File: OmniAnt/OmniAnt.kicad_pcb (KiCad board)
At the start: 4 copper layers, 115 parts, among them J1 Connector, USB-TYPE-C-16P, J10 Conn_01x01, J11 Conn_01x01, J12 Conn_01x01, J13 Conn_01x01, J14 Conn_01x01, J15 Conn_01x01, J16 Conn_01x01, J17 Conn_01x01, J18 Conn_01x01, J19 Conn_01x01, J2 Conn_01x02_Pin, J20 Conn_01x01, J21 Conn_01x01, J22 Conn_01x01, J23 Conn_01x01, J24 Conn_01x01, J25 Conn_01x01, J26 Conn_01x01, J27 Conn_01x01, J28 Conn_01x01, J29 Conn_01x01, J3 Conn_01x04_Pin, J30 Conn_01x01, J31 Conn_01x01, J32 Conn_01x01, J33 Conn_01x01, J34 Conn_01x01, J35 Conn_01x01, J36 Conn_01x01, J37 Conn_01x01, J38 Conn_01x01, J39 Conn_01x01, J4 XT30PW-M, J5 XT30PW-M, J6 XT30PW-M, J7 XT30PW-M, J8 Conn_01x01, J9 Conn_01x01, Q1 NTMFS4C324NT1G, Q10 NTMFS4C324NT1G, Q11 NTMFS4C324NT1G, Q12 NTMFS4C324NT1G, Q2 NTMFS4C324NT1G, Q3 NTMFS4C324NT1G, Q4 NTMFS4C324NT1G, Q5 NTMFS4C324NT1G, Q6 NTMFS4C324NT1G, Q7 NTMFS4C324NT1G, Q8 NTMFS4C324NT1G, Q9 NTMFS4C324NT1G, U1 USBLC6-2P6, U2 TPSM53603RDA, U3 ESP32-S3-WROOM-1, U4 MCF8329A1IREER, U5 MCF8329A1IREER

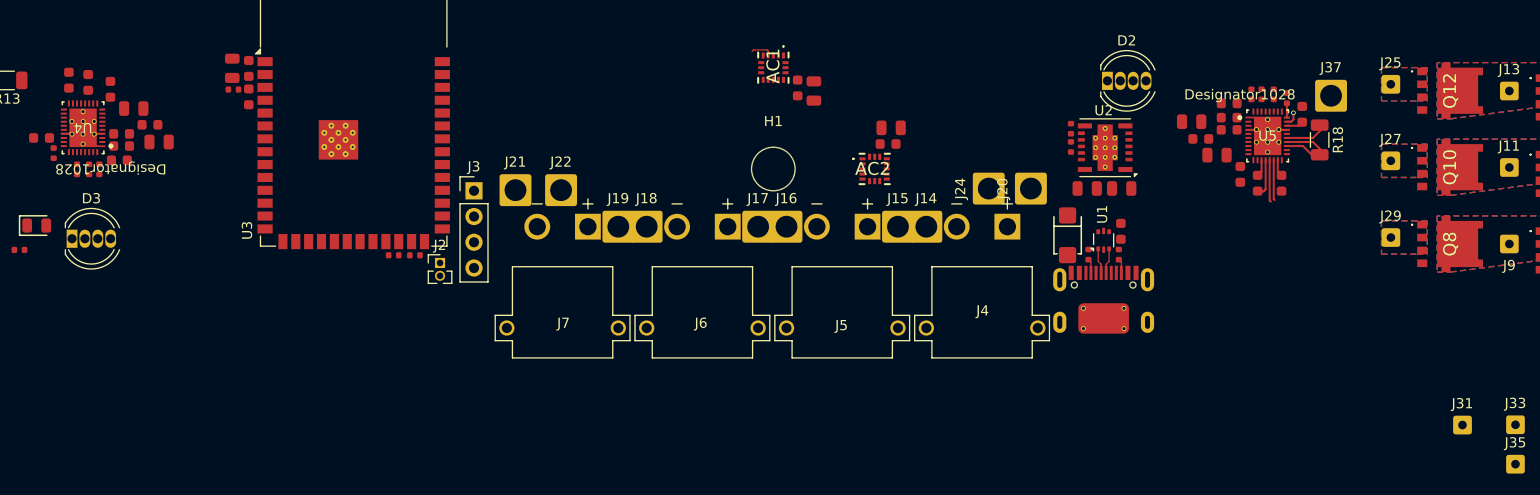
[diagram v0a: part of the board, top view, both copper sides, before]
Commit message: I made more progress on the layout. I'm working on adding the extra protection components to the driver circuit.
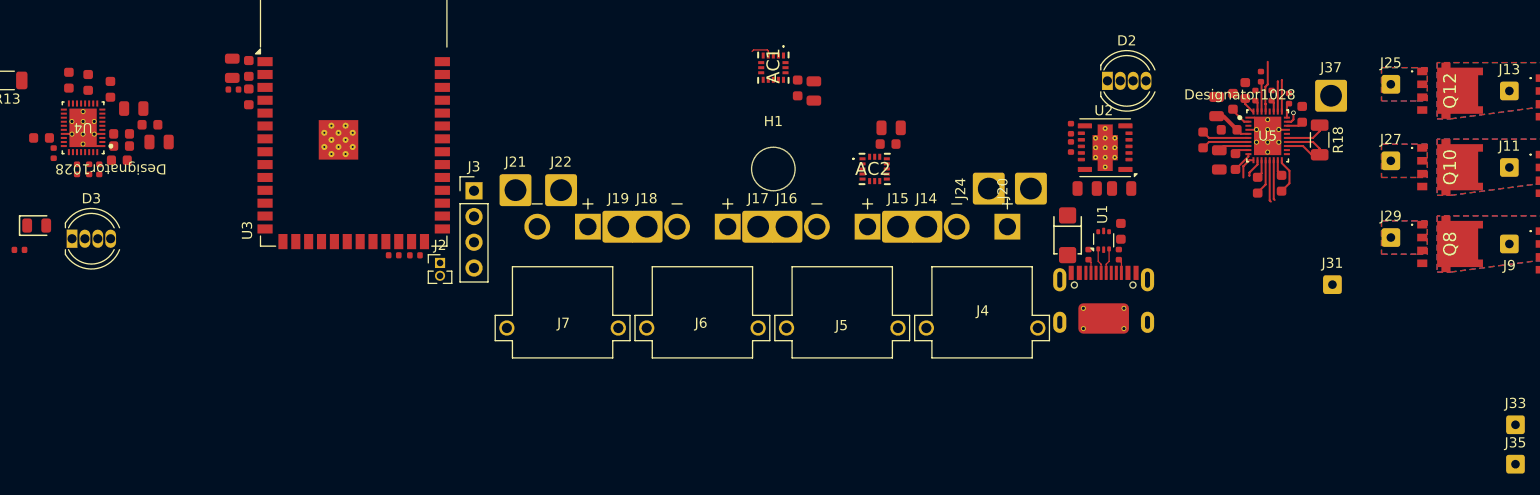
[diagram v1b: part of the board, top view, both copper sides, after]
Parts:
- moved J31 18.9 mm to (257.3, 35.2)
- moved C20 2.88 mm to (245.8, 17.6), turned to 90 degrees
- moved C18 2.03 mm to (248.7, 16.0), turned to 90 degrees
- moved R14 1.75 mm to (250.2, 14.7)
- moved C22 1.66 mm to (247.5, 17.1), turned to 90 degrees
- moved C24 1.36 mm to (247.7, 23.0)
- moved C19 0.52 mm to (246.1, 22.9), turned to -90 degrees
- moved R16 0.41 mm to (249.7, 16.5)
- moved C23 0.25 mm to (244.5, 20.9), turned to 90 degrees
- moved R15 0.24 mm to (251.3, 16.5)
- moved R17 0.21 mm to (253.0, 16.8)
- moved C26 0.19 mm to (249.9, 25.4)
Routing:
- net /Motor2_DAC: track 0.00 -> 5.02 mm
- net Net-(U5-CPL): track 0.00 -> 4.71 mm
- net Net-(U5-CPH): track 0.00 -> 4.71 mm
- net /Batt: track 0.00 -> 3.86 mm
- net /Motor2/PhaseC: track 0.00 -> 3.68 mm
- net /I2C_SDA: track 0.00 -> 3.10 mm
- net Net-(U5-GVDD): track 0.00 -> 3.04 mm
- net /I2C_SCL: track 0.00 -> 2.98 mm
- net Net-(U5-BRAKE): track 0.00 -> 2.97 mm
- net Net-(Q7-G): track 0.00 -> 2.36 mm
- net +3.3V: track 0.00 -> 2.11 mm
- net /Motor2/PhaseA: track 0.00 -> 2.04 mm
- net Net-(Q8-G): track 0.00 -> 1.86 mm
- net Net-(U5-DVDD): track 0.00 -> 1.68 mm
- net Net-(U5-BSTA): track 0.00 -> 1.42 mm
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
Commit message: Ok I did a lot of reading today. I'm going to split each FET into a sheet, so I can add the external circuitry more easily.
I may need to source a different FET. The one I selected has a good EAS, but the rating is only for 11A. and Ideally I would be able to do 19 or 20A. I'm sure I will never do that much current , but relying on the mosfet to handle things seems better than adding an additional tvs diode. Snubber is the way to go for sure to keep things cool.
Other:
- board text added: "TODO: Add mounting / locating holes for the motor. Make the gate traces 0.5mm"
- board text removed: "TODO: Add solder wire connections for the busbar wires. Add mounting / locating holes for the motor. Add boxes to represent the batteries."
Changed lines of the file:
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@@
 		(layer "User.1")
 	)
-	(gr_text "TODO: \nAdd solder wire connections for the busbar wires. \nAdd mounting / locating holes for the motor. \nAdd boxes to represent the batteries. \n"
+	(gr_text "TODO: \nAdd mounting / locating holes for the motor. \nMake the gate traces 0.5mm\n"
 		(at 179.3 173.5 0)
 		(layer "Cmts.User")
@@
 			(font
 				(size 1 1)
-				(thickness 0.15)
+				(thickness 0.125)
 			)
 			(justify left bottom)

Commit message: Well shit making the FETs into libraries totally screwed up the annotation :( I decided to just redo the layout for the FETs anyhow.
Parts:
- removed Q1, Q10, Q11, Q12, Q2, Q3, Q4, Q5, Q6, Q7, Q8, Q9: NTMFS4C324NT1G, Footprints:NVMFS5C442NLWFAFT1G
- added C1001: 470pF, PCM_JLCPCB:C_0603, F.Cu at (9.08, -38.9)
- added C1101: 470pF, PCM_JLCPCB:C_0603, F.Cu at (85.4, 124.3)
- added C1201: 470pF, PCM_JLCPCB:C_0603, F.Cu at (66.6, 161.3)
- added C1301: 470pF, PCM_JLCPCB:C_0603, F.Cu at (-9.68, -20.4)
- added C1401: 470pF, PCM_JLCPCB:C_0603, F.Cu at (-9.68, -38.9)
- added C1501: 470pF, PCM_JLCPCB:C_0603, F.Cu at (66.6, 142.8)
- added C1601: 470pF, PCM_JLCPCB:C_0603, F.Cu at (104.2, 124.3)
- added C1701: 470pF, PCM_JLCPCB:C_0603, F.Cu at (66.6, 179.8)
- added C211: 100nF, PCM_JLCPCB:C_0603, F.Cu at (50.6, -40.8)
- added C212: 100nF, PCM_JLCPCB:C_0603, F.Cu at (50.6, -38.5)
- added C213: 100nF, PCM_JLCPCB:C_0603, F.Cu at (50.6, -36.3)
- added C214: C_US, Capacitor_THT:CP_Radial_D6.3mm_P2.50mm, F.Cu at (43.5, -38.0)
- added C215: C_US, Capacitor_THT:CP_Radial_D6.3mm_P2.50mm, F.Cu at (43.5, -30.1)
- added C216: C_US, Capacitor_THT:CP_Radial_D6.3mm_P2.50mm, F.Cu at (43.5, -22.3)
- added C311: 100nF, PCM_JLCPCB:C_0603, F.Cu at (49.3, 112.3)
- added C312: 100nF, PCM_JLCPCB:C_0603, F.Cu at (49.3, 114.5)
- added C313: 100nF, PCM_JLCPCB:C_0603, F.Cu at (49.3, 116.8)
- added C314: C_US, Capacitor_THT:CP_Radial_D6.3mm_P2.50mm, F.Cu at (42.2, 115.1)
- added C315: C_US, Capacitor_THT:CP_Radial_D6.3mm_P2.50mm, F.Cu at (42.2, 122.9)
- added C316: C_US, Capacitor_THT:CP_Radial_D6.3mm_P2.50mm, F.Cu at (42.2, 130.8)
- added C601: 470pF, PCM_JLCPCB:C_0603, F.Cu at (9.08, -20.4)
- added C701: 470pF, PCM_JLCPCB:C_0603, F.Cu at (-9.68, -57.4)
- added C801: 470pF, PCM_JLCPCB:C_0603, F.Cu at (66.6, 124.3)
- added C901: 470pF, PCM_JLCPCB:C_0603, F.Cu at (9.08, -57.4)
- added D1001: 1N5819WS, PCM_JLCPCB:D_SOD-323, F.Cu at (9.34, -41.5)
- added D1002: SMAJ13A, PCM_JLCPCB:D_SMA, F.Cu at (8.39, -49.8)
- added D1003: SMAJ18CA, PCM_JLCPCB:D_SMA, F.Cu at (8.39, -45.3)
- added D1101: 1N5819WS, PCM_JLCPCB:D_SOD-323, F.Cu at (85.7, 121.7)
- added D1102: SMAJ13A, PCM_JLCPCB:D_SMA, F.Cu at (84.7, 118.0)
- added D1103: SMAJ18CA, PCM_JLCPCB:D_SMA, F.Cu at (84.7, 113.4)
- added D1201: 1N5819WS, PCM_JLCPCB:D_SOD-323, F.Cu at (66.9, 158.7)
- added D1202: SMAJ13A, PCM_JLCPCB:D_SMA, F.Cu at (65.9, 155.0)
- added D1203: SMAJ18CA, PCM_JLCPCB:D_SMA, F.Cu at (65.9, 150.4)
- added D1301: 1N5819WS, PCM_JLCPCB:D_SOD-323, F.Cu at (-9.42, -23.0)
- added D1302: SMAJ13A, PCM_JLCPCB:D_SMA, F.Cu at (-10.4, -31.3)
- added D1303: SMAJ18CA, PCM_JLCPCB:D_SMA, F.Cu at (-10.4, -26.8)
- added D1401: 1N5819WS, PCM_JLCPCB:D_SOD-323, F.Cu at (-9.42, -41.5)
- added D1402: SMAJ13A, PCM_JLCPCB:D_SMA, F.Cu at (-10.4, -45.3)
- added D1403: SMAJ18CA, PCM_JLCPCB:D_SMA, F.Cu at (-10.4, -49.8)
- added D1501: 1N5819WS, PCM_JLCPCB:D_SOD-323, F.Cu at (66.9, 140.2)
- added D1502: SMAJ13A, PCM_JLCPCB:D_SMA, F.Cu at (65.9, 136.5)
- added D1503: SMAJ18CA, PCM_JLCPCB:D_SMA, F.Cu at (65.9, 131.9)
- added D1601: 1N5819WS, PCM_JLCPCB:D_SOD-323, F.Cu at (104.4, 121.7)
- added D1602: SMAJ13A, PCM_JLCPCB:D_SMA, F.Cu at (103.5, 118.0)
- added D1603: SMAJ18CA, PCM_JLCPCB:D_SMA, F.Cu at (103.5, 113.4)
- added D1701: 1N5819WS, PCM_JLCPCB:D_SOD-323, F.Cu at (66.9, 177.2)
- added D1702: SMAJ13A, PCM_JLCPCB:D_SMA, F.Cu at (65.9, 173.5)
- added D1703: SMAJ18CA, PCM_JLCPCB:D_SMA, F.Cu at (65.9, 168.9)
- added D601: 1N5819WS, PCM_JLCPCB:D_SOD-323, F.Cu at (9.34, -23.0)
- added D602: SMAJ13A, PCM_JLCPCB:D_SMA, F.Cu at (8.39, -26.8)
- added D603: SMAJ18CA, PCM_JLCPCB:D_SMA, F.Cu at (8.39, -31.3)
- added D701: 1N5819WS, PCM_JLCPCB:D_SOD-323, F.Cu at (-9.42, -60.0)
- added D702: SMAJ13A, PCM_JLCPCB:D_SMA, F.Cu at (-10.4, -68.3)
- added D703: SMAJ18CA, PCM_JLCPCB:D_SMA, F.Cu at (-10.4, -63.8)
- added D801: 1N5819WS, PCM_JLCPCB:D_SOD-323, F.Cu at (66.9, 121.7)
- added D802: SMAJ13A, PCM_JLCPCB:D_SMA, F.Cu at (65.9, 118.0)
- added D803: SMAJ18CA, PCM_JLCPCB:D_SMA, F.Cu at (65.9, 113.4)
- added D901: 1N5819WS, PCM_JLCPCB:D_SOD-323, F.Cu at (9.34, -60.0)
- added D902: SMAJ13A, PCM_JLCPCB:D_SMA, F.Cu at (8.39, -68.3)
- added D903: SMAJ18CA, PCM_JLCPCB:D_SMA, F.Cu at (8.39, -63.8)
- added QHA701: NTMFS4C324NT1G, Footprints:NVMFS5C442NLWFAFT1G, F.Cu at (-18.8, -65.8)
- added QHA801: NTMFS4C324NT1G, Footprints:NVMFS5C442NLWFAFT1G, F.Cu at (57.5, 116.0)
- added QHB1001: NTMFS4C324NT1G, Footprints:NVMFS5C442NLWFAFT1G, F.Cu at (-0.02, -47.3)
- added QHB1201: NTMFS4C324NT1G, Footprints:NVMFS5C442NLWFAFT1G, F.Cu at (57.5, 153.0)
- added QHC1401: NTMFS4C324NT1G, Footprints:NVMFS5C442NLWFAFT1G, F.Cu at (-18.8, -47.3)
- added QHC1601: NTMFS4C324NT1G, Footprints:NVMFS5C442NLWFAFT1G, F.Cu at (95.1, 116.0)
- added QLA1701: NTMFS4C324NT1G, Footprints:NVMFS5C442NLWFAFT1G, F.Cu at (57.5, 171.5)
- added QLA601: NTMFS4C324NT1G, Footprints:NVMFS5C442NLWFAFT1G, F.Cu at (-0.02, -28.8)
- added QLB1101: NTMFS4C324NT1G, Footprints:NVMFS5C442NLWFAFT1G, F.Cu at (76.3, 116.0)
- added QLB901: NTMFS4C324NT1G, Footprints:NVMFS5C442NLWFAFT1G, F.Cu at (-0.02, -65.8)
- added QLC1301: NTMFS4C324NT1G, Footprints:NVMFS5C442NLWFAFT1G, F.Cu at (-18.8, -28.8)
- added QLC1501: NTMFS4C324NT1G, Footprints:NVMFS5C442NLWFAFT1G, F.Cu at (57.5, 134.5)
- added R1001: 22Ω, PCM_JLCPCB:R_0402, F.Cu at (5.73, -42.1)
- added R1002: 100kΩ, PCM_JLCPCB:R_0402, F.Cu at (5.73, -40.2)
- added R1003: 0Ω, PCM_JLCPCB:R_0402, F.Cu at (5.73, -38.4)
- added R1101: 22Ω, PCM_JLCPCB:R_0402, F.Cu at (82.0, 121.2)
- added R1102: 22Ω, PCM_JLCPCB:R_0402, F.Cu at (82.0, 123.0)
- added R1103: 100kΩ, PCM_JLCPCB:R_0402, F.Cu at (82.0, 124.9)
- added R1104: 0Ω, PCM_JLCPCB:R_0402, F.Cu at (82.0, 126.7)
- added R1201: 22Ω, PCM_JLCPCB:R_0402, F.Cu at (63.3, 158.2)
- added R1202: 22Ω, PCM_JLCPCB:R_0402, F.Cu at (63.3, 160.0)
- added R1203: 100kΩ, PCM_JLCPCB:R_0402, F.Cu at (63.3, 161.9)
- added R1204: 0Ω, PCM_JLCPCB:R_0402, F.Cu at (63.3, 163.7)
- added R1301: 22Ω, PCM_JLCPCB:R_0402, F.Cu at (-13.0, -23.6)
- added R1302: 22Ω, PCM_JLCPCB:R_0402, F.Cu at (-13.0, -21.7)
- added R1303: 100kΩ, PCM_JLCPCB:R_0402, F.Cu at (-13.0, -19.9)
- added R1304: 0Ω, PCM_JLCPCB:R_0402, F.Cu at (-13.0, -18.0)
- added R1401: 22Ω, PCM_JLCPCB:R_0402, F.Cu at (-13.0, -42.1)
- added R1402: 22Ω, PCM_JLCPCB:R_0402, F.Cu at (-13.0, -40.2)
- added R1403: 100kΩ, PCM_JLCPCB:R_0402, F.Cu at (-13.0, -38.4)
- added R1404: 0Ω, PCM_JLCPCB:R_0402, F.Cu at (-13.0, -36.5)
- added R1501: 22Ω, PCM_JLCPCB:R_0402, F.Cu at (63.3, 139.7)
- added R1502: 22Ω, PCM_JLCPCB:R_0402, F.Cu at (63.3, 141.5)
- added R1503: 100kΩ, PCM_JLCPCB:R_0402, F.Cu at (63.3, 143.4)
- added R1504: 0Ω, PCM_JLCPCB:R_0402, F.Cu at (63.3, 145.2)
- added R1601: 22Ω, PCM_JLCPCB:R_0402, F.Cu at (100.8, 121.2)
- added R1602: 22Ω, PCM_JLCPCB:R_0402, F.Cu at (100.8, 123.0)
- added R1603: 100kΩ, PCM_JLCPCB:R_0402, F.Cu at (100.8, 124.9)
- added R1604: 0Ω, PCM_JLCPCB:R_0402, F.Cu at (100.8, 126.7)
- added R1701: 22Ω, PCM_JLCPCB:R_0402, F.Cu at (63.3, 176.7)
- added R1702: 22Ω, PCM_JLCPCB:R_0402, F.Cu at (63.3, 178.5)
- added R1703: 100kΩ, PCM_JLCPCB:R_0402, F.Cu at (63.3, 180.4)
- added R1704: 0Ω, PCM_JLCPCB:R_0402, F.Cu at (63.3, 182.2)
- added R601: 22Ω, PCM_JLCPCB:R_0402, F.Cu at (5.73, -23.6)
- added R602: 22Ω, PCM_JLCPCB:R_0402, F.Cu at (5.73, -21.7)
- added R603: 100kΩ, PCM_JLCPCB:R_0402, F.Cu at (5.73, -19.9)
- added R604: 0Ω, PCM_JLCPCB:R_0402, F.Cu at (5.73, -18.0)
- added R701: 22Ω, PCM_JLCPCB:R_0402, F.Cu at (-13.0, -60.6)
- added R702: 22Ω, PCM_JLCPCB:R_0402, F.Cu at (-13.0, -58.7)
- added R703: 100kΩ, PCM_JLCPCB:R_0402, F.Cu at (-13.0, -56.9)
- added R704: 0Ω, PCM_JLCPCB:R_0402, F.Cu at (-13.0, -55.0)
- added R801: 22Ω, PCM_JLCPCB:R_0402, F.Cu at (63.3, 121.2)
- added R802: 22Ω, PCM_JLCPCB:R_0402, F.Cu at (63.3, 123.0)
- added R803: 100kΩ, PCM_JLCPCB:R_0402, F.Cu at (63.3, 124.9)
- added R804: 0Ω, PCM_JLCPCB:R_0402, F.Cu at (63.3, 126.7)
- added R901: 22Ω, PCM_JLCPCB:R_0402, F.Cu at (5.73, -60.6)
- added R902: 22Ω, PCM_JLCPCB:R_0402, F.Cu at (5.73, -58.7)
- added R903: 100kΩ, PCM_JLCPCB:R_0402, F.Cu at (5.73, -56.9)
- added R904: 0Ω, PCM_JLCPCB:R_0402, F.Cu at (5.73, -55.0)
- added R_ON1001: 22Ω, PCM_JLCPCB:R_0402, F.Cu at (5.73, -36.5)
- renumbered AC1 to AC401, AC2 to AC501, C1 to C101, C2 to C102, C3 to C103, C4 to C104, C5 to C105, C6 to C106, C7 to C201, C8 to C202, C9 to C203, C10 to C204, C11 to C205, C12 to C206, C13 to C207, C14 to C208, C16 to C209, C15 to C210, C17 to C301, C18 to C302, C19 to C303, C20 to C304, C21 to C305, C22 to C306, C23 to C307, C24 to C308, C26 to C309, C25 to C310, C27 to C401, C28 to C402, C29 to C501, C30 to C502, D1 to D101, D2 to D102, D3 to D103, D4 to D104, H5 to H101, H4 to H102, H1 to H103, H2 to H104, H3 to H105, J1 to J101, J2 to J102, J3 to J103, J4 to J104, J5 to J105, J6 to J106, J7 to J107, J14 to J108, J15 to J109, J16 to J110, J17 to J111, J18 to J112, J19 to J113, J21 to J114, J22 to J115, J24 to J116, J20 to J117, J36 to J201, J34 to J202, J30 to J203, J32 to J204, J8 to J205, J10 to J206, J12 to J207, J28 to J208, J26 to J209, J23 to J210, J38 to J211, J37 to J301, J35 to J302, J31 to J303, J33 to J304, J9 to J305, J11 to J306, J13 to J307, J29 to J308, J27 to J309, J25 to J310, J39 to J311, R1 to R101, R2 to R102, R3 to R103, R4 to R104, R5 to R105, R6 to R106, R7 to R107, R8 to R108, R9 to R201, R10 to R202, R11 to R203, R12 to R204, R13 to R205, R14 to R301, R15 to R302, R16 to R303, R17 to R304, R18 to R305, U1 to U101, U2 to U102, U3 to U103, U4 to U201, U5 to U301
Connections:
- C208 pad 1: Net-(U4-BSTA) -> /Motor1/PhaseA
- C208 pad 2: /Motor1/PhaseA -> Net-(U201-BSTA)
- C209 pad 1: Net-(U4-BSTB) -> /Motor1/PhaseB
- C209 pad 2: /Motor1/PhaseB -> Net-(U201-BSTB)
- C210 pad 1: Net-(U4-BSTC) -> /Motor1/PhaseC
- C210 pad 2: /Motor1/PhaseC -> Net-(U201-BSTC)
- C308 pad 1: Net-(U5-BSTA) -> /Motor2/PhaseA
- C308 pad 2: /Motor2/PhaseA -> Net-(U301-BSTA)
- C309 pad 1: Net-(U5-BSTB) -> /Motor2/PhaseB
- C309 pad 2: /Motor2/PhaseB -> Net-(U301-BSTB)
- C310 pad 1: Net-(U5-BSTC) -> /Motor2/PhaseC
- C310 pad 2: /Motor2/PhaseC -> Net-(U301-BSTC)
- U201 pad 11: Net-(Q1-G) -> /Motor1/QHA/G
- U201 pad 12: Net-(Q2-G) -> /Motor1/QLA/G
- U201 pad 13: Net-(U4-BSTB) -> Net-(U201-BSTB)
- U201 pad 15: Net-(Q3-G) -> /Motor1/QHB/G
- U201 pad 16: Net-(Q4-G) -> /Motor1/QLB/G
- U201 pad 17: Net-(U4-BSTC) -> Net-(U201-BSTC)
- U201 pad 19: Net-(Q5-G) -> /Motor1/QHC/G
- U201 pad 20: Net-(Q6-G) -> /Motor1/QLC/G
- U201 pad 9: Net-(U4-BSTA) -> Net-(U201-BSTA)
- U301 pad 11: Net-(Q7-G) -> /Motor2/QHA/G
- U301 pad 12: Net-(Q8-G) -> /Motor2/QLA/G
- U301 pad 13: Net-(U5-BSTB) -> Net-(U301-BSTB)
- U301 pad 15: Net-(Q9-G) -> /Motor2/QHB/G
- U301 pad 16: Net-(Q10-G) -> /Motor2/QLB/G
- U301 pad 17: Net-(U5-BSTC) -> Net-(U301-BSTC)
- U301 pad 19: Net-(Q11-G) -> /Motor2/QHC/G
- U301 pad 20: Net-(Q12-G) -> /Motor2/QLC/G
- U301 pad 9: Net-(U5-BSTA) -> Net-(U301-BSTA)
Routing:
- net Net-(Q9-G): track 4.14 -> 0.00 mm
- net /Motor2/QHB/G: track 0.00 -> 4.14 mm
- net Net-(Q10-G): track 3.97 -> 0.00 mm
- net /Motor2/QLB/G: track 0.00 -> 3.97 mm
- net Net-(Q7-G): track 2.36 -> 0.00 mm
- net /Motor2/QHA/G: track 0.00 -> 2.36 mm
- net Net-(Q8-G): track 1.86 -> 0.00 mm
- net /Motor2/QLA/G: track 0.00 -> 1.86 mm
- net Net-(U5-BSTB): track 1.84 -> 0.00 mm
- net /Motor2/PhaseB: track 3.53 -> 5.38 mm
- net /Motor2/PhaseC: track 3.68 -> 5.33 mm
- net Net-(U5-BSTC): track 1.65 -> 0.00 mm
- net Net-(U5-BSTA): track 1.42 -> 0.00 mm
- net /Motor2/PhaseA: track 2.04 -> 3.46 mm

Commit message: Really good progress today. I got all the FETs placed again and routed. I'm working on the pours for the FETs now.
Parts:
- added C105: 47uF, PCM_JLCPCB:C_1206, F.Cu at (159.9, 95.8)
- added C106: 47uF, PCM_JLCPCB:C_1206, F.Cu at (159.9, 99.2)
- added D105: D_Zener, PCM_JLCPCB:D_SOD-123FL, F.Cu at (159.8, 102.5)
- R1003, R1104, R1204, R1304, R1404, R1504, R1604, R1704, R604, R704, R804, R904: footprint PCM_JLCPCB:R_0402 -> PCM_JLCPCB:R_0603
- moved C311 280.3 mm to (254.1, -79.2)
- moved C312 280.3 mm to (254.1, -76.9)
- moved C313 280.3 mm to (254.1, -74.7)
- moved C314 280.3 mm to (247.0, -76.4)
- moved C315 280.3 mm to (247.0, -68.5)
- moved C316 280.3 mm to (247.0, -60.7)
- moved R704 274.8 mm to (226.5, 79.8)
- moved R1204 270.9 mm to (297.1, 27.0), turned to 180 degrees
- moved Q1201 267.3 mm to (297.3, 34.9), turned to -90 degrees
- moved C1201 264.4 mm to (294.4, 27.0), turned to 180 degrees
- moved R904 263.5 mm to (232.1, 79.8)
- moved R1304 262.0 mm to (226.5, 88.3)
- moved R1704 261.6 mm to (282.0, 38.6), turned to 180 degrees
- moved D1203 259.6 mm to (295.6, 29.4)
- moved R1203 258.4 mm to (289.2, 36.4), turned to 90 degrees
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- renumbered C105 to C107, C106 to C108, QLB1101 to Q1101, QHB1201 to Q1201, QLC1501 to Q1501, QHC1601 to Q1601, QLA1701 to Q1701, QHA801 to Q801
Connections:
- U101 pad 1: Net-(J101-D+-PadA6) -> /D-
- U101 pad 2: /VUSB -> GND
- U101 pad 3: Net-(J101-D--PadA7) -> /D+
- U101 pad 4: /D- -> Net-(J101-D+-PadA6)
- U101 pad 5: GND -> /VUSB
- U101 pad 6: /D+ -> Net-(J101-D--PadA7)
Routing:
- net /Motor2/LSS: track 7.70 -> 14.2 mm
- net /Batt: track 3.86 -> 6.86 mm
- net /Motor1/PhaseC: track 0.00 -> 2.23 mm
- net /Motor2/PhaseA: track 3.46 -> 5.67 mm
- net /Motor2/QLA/G: track 1.86 -> 4.08 mm
- net /Motor2/QHB/G: track 4.14 -> 6.35 mm
- net /Motor2/QLB/G: track 3.97 -> 6.18 mm
- net /Motor2/QLC/G: track 0.00 -> 2.21 mm
- net /Motor2/QHC/G: track 0.00 -> 2.21 mm
- net /Motor2/QHA/G: track 2.36 -> 4.57 mm
- net /SPI1_SCK: track 2.16 -> 0.00 mm
- net Net-(U301-BSTB): track 0.00 -> 1.84 mm
- net Net-(U301-BSTC): track 0.00 -> 1.39 mm
- net Net-(D1401-Pad1): track 0.00 -> 1.01 mm
- added copper zone on B.Cu, net Net-(C1101-Pad1)
- added copper zone on F.Cu, net Net-(C1101-Pad1)
- added copper zone on In1.Cu, net Net-(C1101-Pad1)
- added copper zone on In2.Cu, net Net-(C1101-Pad1)
- added copper zone on B.Cu, net Net-(C1201-Pad1)
- added copper zone on F.Cu, net Net-(C1201-Pad1)
- added copper zone on In1.Cu, net Net-(C1201-Pad1)
- added copper zone on In2.Cu, net Net-(C1201-Pad1)
- added copper zone on B.Cu, net Net-(C1401-Pad1)
- added copper zone on F.Cu, net Net-(C1401-Pad1)
- added copper zone on In1.Cu, net Net-(C1401-Pad1)
- added copper zone on In2.Cu, net Net-(C1401-Pad1)
- added copper zone on B.Cu, net Net-(C1501-Pad1)
- added copper zone on F.Cu, net Net-(C1501-Pad1)
- added copper zone on In1.Cu, net Net-(C1501-Pad1)
- added copper zone on In2.Cu, net Net-(C1501-Pad1)
- added copper zone on B.Cu, net Net-(C1601-Pad1)
- added copper zone on F.Cu, net Net-(C1601-Pad1)
- added copper zone on In1.Cu, net Net-(C1601-Pad1)
- added copper zone on In2.Cu, net Net-(C1601-Pad1)
- added copper zone on B.Cu, net Net-(C1701-Pad1)
- added copper zone on F.Cu, net Net-(C1701-Pad1)
- added copper zone on In1.Cu, net Net-(C1701-Pad1)
- added copper zone on In2.Cu, net Net-(C1701-Pad1)
- added copper zone on B.Cu, net Net-(C801-Pad1)
- added copper zone on F.Cu, net Net-(C801-Pad1)
- added copper zone on In1.Cu, net Net-(C801-Pad1)
- added copper zone on In2.Cu, net Net-(C801-Pad1)
- added copper zone on B.Cu, net Net-(D1101-Pad1)
- added copper zone on F.Cu, net Net-(D1101-Pad1)
- added copper zone on In1.Cu, net Net-(D1101-Pad1)
- added copper zone on In2.Cu, net Net-(D1101-Pad1)
- added copper zone on B.Cu, net Net-(D1201-Pad1)
- added copper zone on F.Cu, net Net-(D1201-Pad1)
- added copper zone on In1.Cu, net Net-(D1201-Pad1)
- added copper zone on In2.Cu, net Net-(D1201-Pad1)
- added copper zone on B.Cu, net Net-(D1501-Pad1)
- added copper zone on F.Cu, net Net-(D1501-Pad1)
- added copper zone on In1.Cu, net Net-(D1501-Pad1)
- added copper zone on In2.Cu, net Net-(D1501-Pad1)
- added copper zone on B.Cu, net Net-(D1601-Pad1)
- added copper zone on F.Cu, net Net-(D1601-Pad1)
- added copper zone on In1.Cu, net Net-(D1601-Pad1)
- added copper zone on In2.Cu, net Net-(D1601-Pad1)
- added copper zone on B.Cu, net Net-(D1701-Pad1)
- added copper zone on F.Cu, net Net-(D1701-Pad1)
- added copper zone on In1.Cu, net Net-(D1701-Pad1)
- added copper zone on In2.Cu, net Net-(D1701-Pad1)
- added copper zone on B.Cu, net Net-(D801-Pad1)
- added copper zone on F.Cu, net Net-(D801-Pad1)
- added copper zone on In1.Cu, net Net-(D801-Pad1)
- added copper zone on In2.Cu, net Net-(D801-Pad1)
- added copper zone on B.Cu, net Net-(Q1101-G)
- added copper zone on F.Cu, net Net-(Q1101-G)
- added copper zone on In1.Cu, net Net-(Q1101-G)
- added copper zone on In2.Cu, net Net-(Q1101-G)
- added copper zone on B.Cu, net Net-(Q1201-G)
- added copper zone on F.Cu, net Net-(Q1201-G)
- added copper zone on In1.Cu, net Net-(Q1201-G)
- added copper zone on In2.Cu, net Net-(Q1201-G)
- added copper zone on B.Cu, net Net-(Q1501-G)
- added copper zone on F.Cu, net Net-(Q1501-G)
- added copper zone on In1.Cu, net Net-(Q1501-G)
- added copper zone on In2.Cu, net Net-(Q1501-G)
- added copper zone on B.Cu, net Net-(Q1601-G)
- added copper zone on F.Cu, net Net-(Q1601-G)
- added copper zone on In1.Cu, net Net-(Q1601-G)
- added copper zone on In2.Cu, net Net-(Q1601-G)
- added copper zone on B.Cu, net Net-(Q1701-G)
- added copper zone on F.Cu, net Net-(Q1701-G)
- added copper zone on In1.Cu, net Net-(Q1701-G)
- added copper zone on In2.Cu, net Net-(Q1701-G)
- added copper zone on B.Cu, net Net-(Q801-G)
- added copper zone on F.Cu, net Net-(Q801-G)
- added copper zone on In1.Cu, net Net-(Q801-G)
- added copper zone on In2.Cu, net Net-(Q801-G)
- added copper zone on B.Cu, net Net-(QHC1401-G)
- added copper zone on F.Cu, net Net-(QHC1401-G)
- added copper zone on In1.Cu, net Net-(QHC1401-G)
- added copper zone on In2.Cu, net Net-(QHC1401-G)
- removed copper zone on B.Cu, net /Motor2/LSS
- removed copper zone on F.Cu, net /Motor2/LSS
- removed copper zone on In1.Cu, net /Motor2/LSS
- removed copper zone on In2.Cu, net /Motor2/LSS
- removed copper zone on B.Cu, net /Motor2/PhaseA
- removed copper zone on F.Cu, net /Motor2/PhaseA
- removed copper zone on In1.Cu, net /Motor2/PhaseA
- removed copper zone on In2.Cu, net /Motor2/PhaseA
- removed copper zone on B.Cu, net /Motor2/PhaseB
- removed copper zone on F.Cu, net /Motor2/PhaseB
- removed copper zone on In1.Cu, net /Motor2/PhaseB
- removed copper zone on In2.Cu, net /Motor2/PhaseB
- removed copper zone on B.Cu, net /Motor2/PhaseC
- removed copper zone on F.Cu, net /Motor2/PhaseC
- removed copper zone on In1.Cu, net /Motor2/PhaseC
- removed copper zone on In2.Cu, net /Motor2/PhaseC

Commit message: I di some good work breaking out the traces around the gate driver. Unfortunatly when I went to connect the driver upto the FET array I noticed that I needed to reorder where the phase came out. To do that I needed to change the gate resistor size to make room to pull the phase through which caused a large tearup. I'm still working through it.
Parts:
- removed R_ON1001: 22Ω, PCM_JLCPCB:R_0402
- added J104: Conn_01x02_Pin, Connector_PinHeader_1.27mm:PinHeader_1x02_P1.27mm_Vertical, F.Cu at (215.9, 56.1)
- added J105: Conn_01x02_Pin, Connector_PinHeader_1.27mm:PinHeader_1x02_P1.27mm_Vertical, F.Cu at (211.8, 56.1)
- added R1002: 22Ω, PCM_JLCPCB:R_0805, F.Cu at (248.8, -23.7)
- R1001, R1101, R1102, R1201, R1202, R1301, R1302, R1401, R1402, R1501, R1502, R1601, R1602, R1701, R1702, R601, R602, R701, R702, R801, R802, R901, R902: footprint PCM_JLCPCB:R_0402 -> PCM_JLCPCB:R_0805
- moved R1301 268.4 mm to (255.2, -34.6)
- moved R1302 268.4 mm to (255.2, -31.6)
- moved R601 249.4 mm to (255.2, -26.7)
- moved R602 249.4 mm to (255.2, -23.7)
- moved R701 246.4 mm to (232.9, -44.5)
- moved R1001 243.5 mm to (248.8, -26.7)
- moved R902 239.2 mm to (242.3, -23.7)
- moved R901 239.0 mm to (242.3, -26.7)
- moved R702 238.1 mm to (224.7, -44.3)
- moved R1402 162.5 mm to (248.8, -31.6), turned to 0 degrees
- moved R1401 162.1 mm to (248.8, -34.6)
- moved C311 128.1 mm to (295.7, 41.9), turned to 180 degrees
- moved C316 125.3 mm to (303.7, 51.0)
- moved C315 119.7 mm to (303.7, 36.8)
- moved C314 114.1 mm to (303.7, 22.7)
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- renumbered J104 to J106, J105 to J107, J106 to J108, J107 to J109, J108 to J110, J109 to J111, J110 to J112, J111 to J113, J112 to J114, J113 to J115, J114 to J116, J115 to J117, J116 to J118, J117 to J119, R1002 to R1003, R1003 to R1004
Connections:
- R1001 pad 2: Net-(D1001-Pad1) -> Net-(QHB1001-G)
- U301 pad 29: /I2C_SDA -> /Motor2/I2C_SDA
- U301 pad 30: /I2C_SCL -> /Motor2/I2C_SCL
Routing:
- net /Motor2/LSS: track 14.2 -> 59.4 mm
- net /Motor2/QHC/G: track 2.21 -> 23.9 mm
- net /Motor2/PhaseC: track 5.64 -> 19.0 mm
- net /Motor2/QLA/G: track 4.08 -> 11.0 mm
- net /Motor2/QLC/G: track 2.21 -> 8.19 mm
- net /Motor2_DAC: track 5.02 -> 0.00 mm
- net /Motor2/QLB/G: track 6.18 -> 10.6 mm
- net /Motor2/QHB/G: track 6.35 -> 2.47 mm
- net /I2C_SDA: track 3.10 -> 0.00 mm
- net /I2C_SCL: track 2.98 -> 0.00 mm
- net (no net): track 0.00 -> 2.41 mm
- net /Motor2/PhaseA: track 5.67 -> 3.36 mm
- net /Motor2/QHA/G: track 4.57 -> 2.47 mm
- net Net-(U301-BSTB): track 1.84 -> 0.00 mm
- net Net-(J101-D--PadA7): track 2.48 -> 0.85 mm
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- added copper zone on F.Cu, net /Motor2/LSS
- added copper zone on In1.Cu, net /Motor2/LSS
- added copper zone on In2.Cu, net /Motor2/LSS
- added copper zone on B.Cu, net /Motor2/PhaseA
- added copper zone on F.Cu, net /Motor2/PhaseA
- added copper zone on In1.Cu, net /Motor2/PhaseA
- added copper zone on In2.Cu, net /Motor2/PhaseA
- added copper zone on B.Cu, net /Motor2/PhaseB
- added copper zone on F.Cu, net /Motor2/PhaseB
- added copper zone on In1.Cu, net /Motor2/PhaseB
- added copper zone on In2.Cu, net /Motor2/PhaseB
- added copper zone on B.Cu, net /Motor2/PhaseC
- added copper zone on F.Cu, net /Motor2/PhaseC
- added copper zone on In1.Cu, net /Motor2/PhaseC
- added copper zone on In2.Cu, net /Motor2/PhaseC
- added copper zone on F.Cu, net /Motor2/QHA/G
- added copper zone on F.Cu, net /Motor2/QHB/G
- added copper zone on F.Cu, net /Motor2/QHC/G
- added copper zone on F.Cu, net /Motor2/QLA/G
- added copper zone on F.Cu, net /Motor2/QLB/G
- added copper zone on F.Cu, net /Motor2/QLC/G
- added copper zone on F.Cu, net Net-(U301-BSTB)
- added copper zone on F.Cu, net Net-(U301-BSTC)
- removed copper zone on B.Cu, net Net-(Q1101-G)
- removed copper zone on In1.Cu, net Net-(Q1101-G)
- removed copper zone on In2.Cu, net Net-(Q1101-G)
- removed copper zone on B.Cu, net Net-(Q1201-G)
- removed copper zone on In1.Cu, net Net-(Q1201-G)
- removed copper zone on In2.Cu, net Net-(Q1201-G)
- removed copper zone on B.Cu, net Net-(Q1501-G)
- removed copper zone on In1.Cu, net Net-(Q1501-G)
- removed copper zone on In2.Cu, net Net-(Q1501-G)
- removed copper zone on B.Cu, net Net-(Q1601-G)
- removed copper zone on In1.Cu, net Net-(Q1601-G)
- removed copper zone on In2.Cu, net Net-(Q1601-G)
- removed copper zone on B.Cu, net Net-(Q1701-G)
- removed copper zone on In1.Cu, net Net-(Q1701-G)
- removed copper zone on In2.Cu, net Net-(Q1701-G)
- removed copper zone on B.Cu, net Net-(Q801-G)
- removed copper zone on In1.Cu, net Net-(Q801-G)
- removed copper zone on In2.Cu, net Net-(Q801-G)
